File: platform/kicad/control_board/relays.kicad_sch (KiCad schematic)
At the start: 12 parts, among them K1 LCA717, K2 LCA717, K3 LCA717, K4 LCA717

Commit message: Controller: Upsize resistors
This change alters the resistor footprints from 0201 to 0603 which allows the cheaper
PCBA method to be used, decreasing the cost of the board.
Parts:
- R16, R22, R23, R24: footprint Resistor_SMD:R_0201_0603Metric -> Resistor_SMD:R_0603_1608Metric
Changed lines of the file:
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@@
 			)
 		)
-		(property "Footprint" "Resistor_SMD:R_0201_0603Metric"
+		(property "Footprint" "Resistor_SMD:R_0603_1608Metric"
 			(at 116.84 88.138 90)
 			(effects
@@
 			)
 		)
-		(property "Footprint" "Resistor_SMD:R_0201_0603Metric"
+		(property "Footprint" "Resistor_SMD:R_0603_1608Metric"
 			(at 116.84 103.378 90)
 			(effects
@@
 			)
 		)
-		(property "Footprint" "Resistor_SMD:R_0201_0603Metric"
+		(property "Footprint" "Resistor_SMD:R_0603_1608Metric"
 			(at 116.84 118.618 90)
 			(effects
@@
 			)
 		)
-		(property "Footprint" "Resistor_SMD:R_0201_0603Metric"
+		(property "Footprint" "Resistor_SMD:R_0603_1608Metric"
 			(at 116.84 71.628 90)
 			(effects

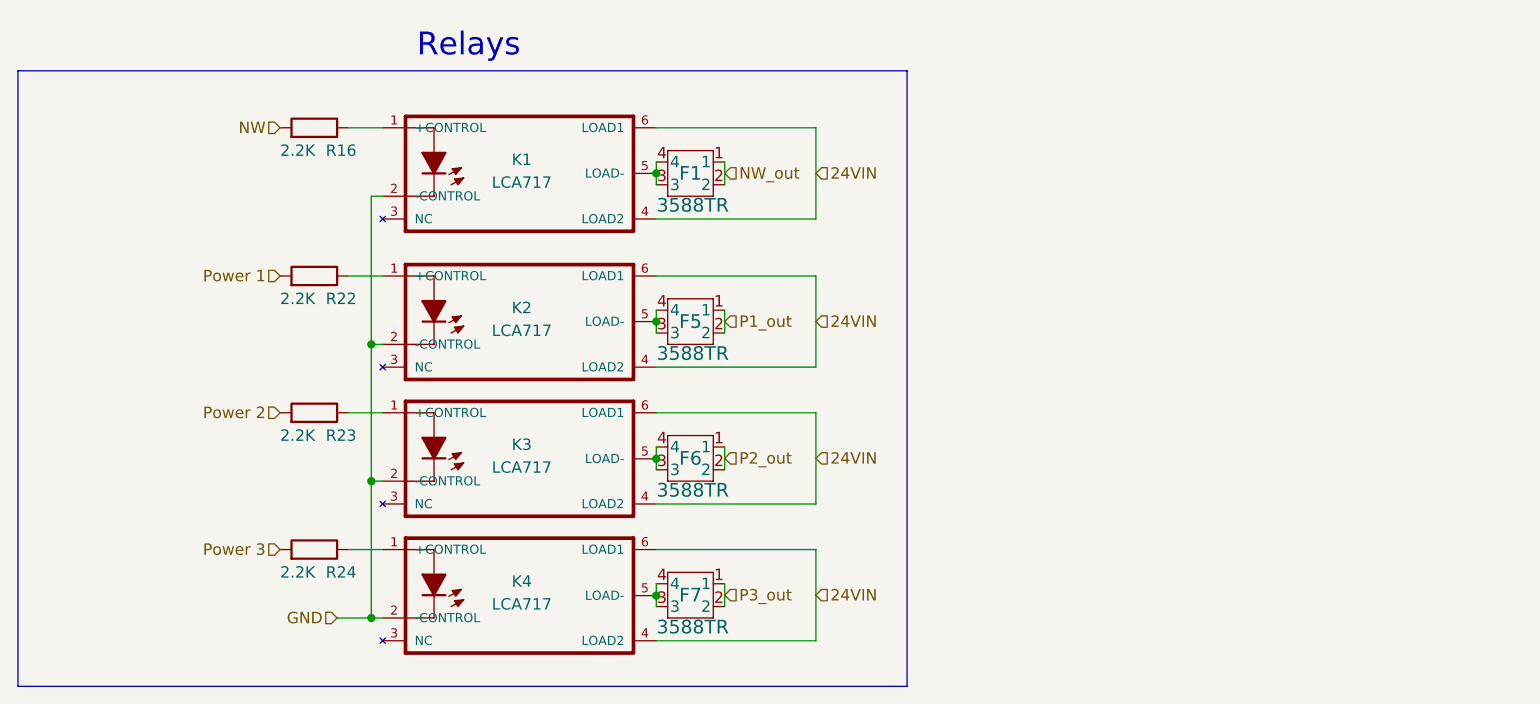
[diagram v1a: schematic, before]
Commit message: Controller: Move fuse before relay and add test points (#21)
This change moves the fuse before the relay to prevent the relay from still being powered (and potentially short circuit)
after the fuse has blow. This change also adds LED indicators for the relay status, as well as adding test points for
the control signal of each relay.
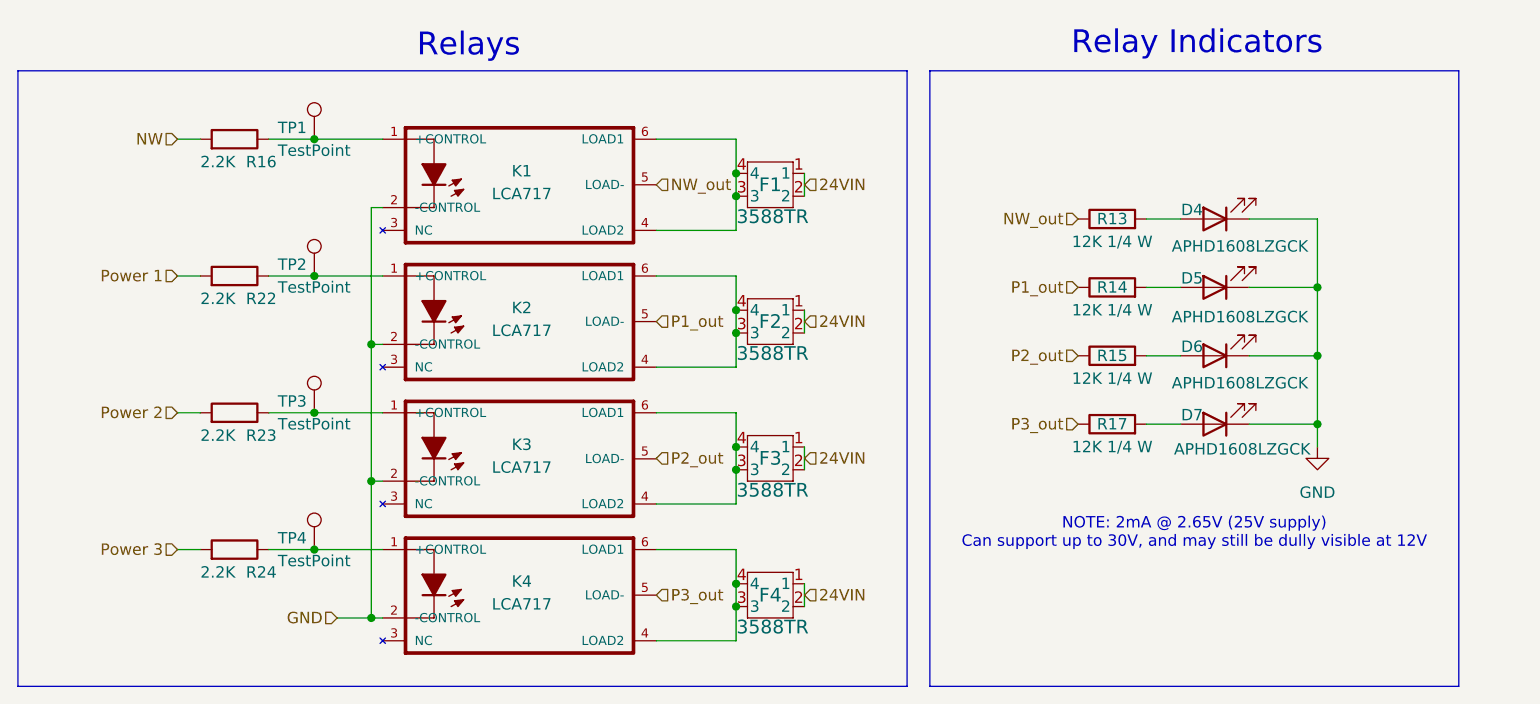
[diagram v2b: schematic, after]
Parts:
- removed F6, F7: 3588TR, AusOcean:3588TR_FUSE_HOLDER, symbol AusOcean:3588TR
- added D4, D5, D6, D7: APHD1608LZGCK, LED_SMD:LED_0603_1608Metric, symbol Device:LED
- added F3, F4: 3588TR, AusOcean:3588TR_FUSE_HOLDER, symbol AusOcean:3588TR
- added R13, R14, R15, R17: 12K 1/4 W, Resistor_SMD:R_0603_1608Metric, symbol Device:R
- added TP1, TP2, TP3, TP4: TestPoint, TestPoint:TestPoint_THTPad_D1.0mm_Drill0.5mm, symbol Connector:TestPoint
- renumbered F5 to F2
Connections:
- net 24VIN: now also F1.1, F1.2, F2.1, F2.2, F3.1, F3.2, F4.1, F4.2; no longer K1.4 (LOAD2), K1.6 (LOAD1), K2.4 (LOAD2), K2.6 (LOAD1), K3.4 (LOAD2), K3.6 (LOAD1), K4.4 (LOAD2), K4.6 (LOAD1)
- net GND: now also D4.1 (K), D5.1 (K), D6.1 (K), D7.1 (K)
- net NW_out: now also K1.5 (LOAD-), R13.1; no longer F1.1, F1.2
- net P1_out: now also K2.5 (LOAD-), R14.1; no longer F2.1, F2.2
- net P2_out: now also K3.5 (LOAD-), R15.1
- net P3_out: now also K4.5 (LOAD-), R17.1
- net at F2.3, F2.4: now also K2.4 (LOAD2), K2.6 (LOAD1); no longer K2.5 (LOAD-)
- net at K2.1 (+CONTROL), R22.1: now also TP2.1
- net at K3.1 (+CONTROL), R23.1: now also TP3.1
- net at K4.1 (+CONTROL), R24.1: now also TP4.1
- net at K1.1 (+CONTROL), R16.1: now also TP1.1
- net at F1.3, F1.4: now also K1.4 (LOAD2), K1.6 (LOAD1); no longer K1.5 (LOAD-)
- new net: D5.2 (A), R14.2
- new net: F3.3, F3.4, K3.4 (LOAD2), K3.6 (LOAD1)
- new net: F4.3, F4.4, K4.4 (LOAD2), K4.6 (LOAD1)
- new net: D6.2 (A), R15.2
- new net: D7.2 (A), R17.2
- new net: D4.2 (A), R13.2
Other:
- note added: "NOTE: 2mA @ 2.65V (25V supply) Can support up to 30V, and may still be dully visible at 12V"
- note added: "Relay Indicators"
- moved on the sheet: F2, K1, R16, R22, R23, R24
